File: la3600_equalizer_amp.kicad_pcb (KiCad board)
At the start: 2 copper layers, 90.9 x 174.8 mm, 70 parts, among them J1 JACK_TRS_3PINS, J2 JACK_TRS_3PINS, J3 Conn_01x03, Q1 BD139, Q2 BD140, Q3 BD139, Q4 BD140, U1 LA3600, U2 LA3600, U3 NE5532

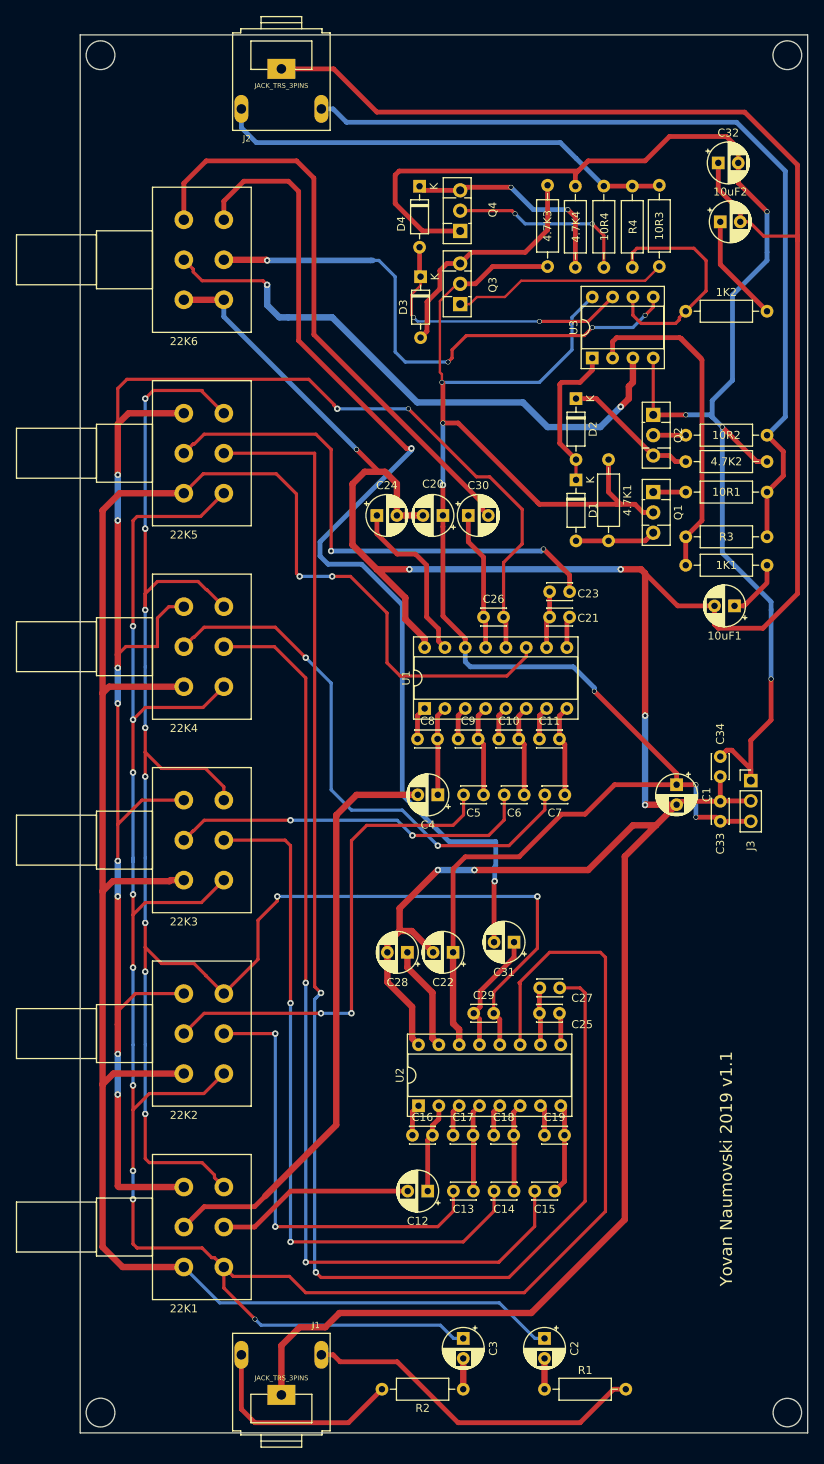
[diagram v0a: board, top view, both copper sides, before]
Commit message: add proper mounting holes (M3)
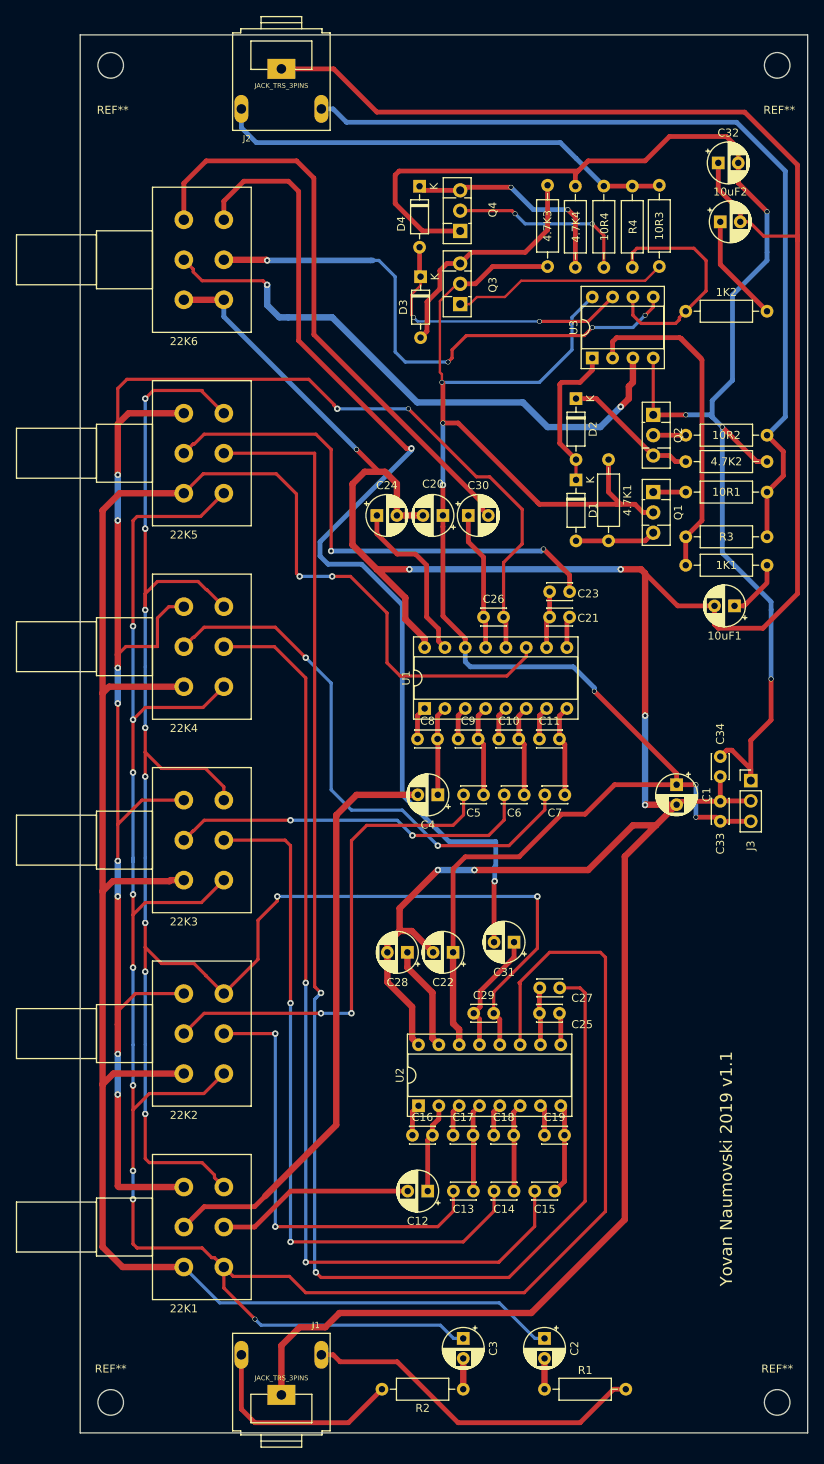
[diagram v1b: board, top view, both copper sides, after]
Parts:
- added REF**: MountingHole_3.2mm_M3, MountingHole:MountingHole_3.2mm_M3, F.Cu at (27.7, 28.4)
- added REF**: MountingHole_3.2mm_M3, MountingHole:MountingHole_3.2mm_M3, F.Cu at (111.0, 28.4)
- added REF**: MountingHole_3.2mm_M3, MountingHole:MountingHole_3.2mm_M3, F.Cu at (111.0, 195.6)
- added REF**: MountingHole_3.2mm_M3, MountingHole:MountingHole_3.2mm_M3, F.Cu at (27.7, 195.6)
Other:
- outline, holes or cut-outs redrawn
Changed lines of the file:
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@@
   (general
     (thickness 1.6)
-    (drawings 9)
+    (drawings 5)
     (tracks 761)
     (zones 0)
-    (modules 70)
+    (modules 74)
     (nets 66)
   )
@@
     )
   )
-  (gr_circle (center 112.268 196.85) (end 112.268 198.628) (layer Edge.Cuts) (width 0.15))
-  (gr_circle (center 26.416 196.85) (end 26.162 198.628) (layer Edge.Cuts) (width 0.15))
-  (gr_circle (center 112.268 27.178) (end 113.538 25.908) (layer Edge.Cuts) (width 0.15))
-  (gr_circle (center 26.416 27.178) (end 25.146 25.908) (layer Edge.Cuts) (width 0.15))
+  (module MountingHole:MountingHole_3.2mm_M3 (layer F.Cu)
+    (at 27.686 28.448)
+    (descr "Mounting Hole 3.2mm, no annular, M3")
+    (tags "mounting hole 3.2mm no annular m3")
+    (attr virtual)
+    (fp_text reference REF** (at 0.254 5.588) (layer F.SilkS)
+      (effects (font (size 1 1) (thickness 0.15)))
+    )
+    (fp_text value MountingHole_3.2mm_M3 (at 0 4.2) (layer F.Fab)
+      (effects (font (size 1 1) (thickness 0.15)))
+    )
+    (fp_circle (center 0 0) (end 3.45 0) (layer F.CrtYd) (width 0.05))
+    (fp_circle (center 0 0) (end 3.2 0) (layer Cmts.User) (width 0.15))
+    (fp_text user %R (at 0.3 0) (layer F.Fab)
+      (effects (font (size 1 1) (thickness 0.15)))
+    )
+    (pad 1 np_thru_hole circle (at 0 0) (size 3.2 3.2) (drill 3.2) (layers *.Cu *.Mask))
+  )
+  (module MountingHole:MountingHole_3.2mm_M3 (layer F.Cu)
+    (at 110.998 28.448)
+    (descr "Mounting Hole 3.2mm, no annular, M3")
+    (tags "mounting hole 3.2mm no annular m3")
+    (attr virtual)
+    (fp_text reference REF** (at 0.254 5.588) (layer F.SilkS)
+      (effects (font (size 1 1) (thickness 0.15)))
+    )
+    (fp_text value MountingHole_3.2mm_M3 (at 0 4.2) (layer F.Fab)
+      (effects (font (size 1 1) (thickness 0.15)))
+    )
+    (fp_circle (center 0 0) (end 3.45 0) (layer F.CrtYd) (width 0.05))
+    (fp_circle (center 0 0) (end 3.2 0) (layer Cmts.User) (width 0.15))
+    (fp_text user %R (at 0.3 0) (layer F.Fab)
+      (effects (font (size 1 1) (thickness 0.15)))
+    )
+    (pad 1 np_thru_hole circle (at 0 0) (size 3.2 3.2) (drill 3.2) (layers *.Cu *.Mask))
+  )
+  (module MountingHole:MountingHole_3.2mm_M3 (layer F.Cu)
+    (at 110.998 195.58)
+    (descr "Mounting Hole 3.2mm, no annular, M3")
+    (tags "mounting hole 3.2mm no annular m3")
+    (attr virtual)
+    (fp_text reference REF** (at 0 -4.2) (layer F.SilkS)
+      (effects (font (size 1 1) (thickness 0.15)))
+    )
+    (fp_text value MountingHole_3.2mm_M3 (at 0 4.2) (layer F.Fab)
+      (effects (font (size 1 1) (thickness 0.15)))
+    )
+    (fp_circle (center 0 0) (end 3.45 0) (layer F.CrtYd) (width 0.05))
+    (fp_circle (center 0 0) (end 3.2 0) (layer Cmts.User) (width 0.15))
+    (fp_text user %R (at 0.3 0) (layer F.Fab)
+      (effects (font (size 1 1) (thickness 0.15)))
+    )
+    (pad 1 np_thru_hole circle (at 0 0) (size 3.2 3.2) (drill 3.2) (layers *.Cu *.Mask))
+  )
+  (module MountingHole:MountingHole_3.2mm_M3 (layer F.Cu)
+    (at 27.686 195.58)
+    (descr "Mounting Hole 3.2mm, no annular, M3")
+    (tags "mounting hole 3.2mm no annular m3")
+    (attr virtual)
+    (fp_text reference REF** (at 0 -4.2) (layer F.SilkS)
+      (effects (font (size 1 1) (thickness 0.15)))
+    )
+    (fp_text value MountingHole_3.2mm_M3 (at 0 4.2) (layer F.Fab)
+      (effects (font (size 1 1) (thickness 0.15)))
+    )
+    (fp_circle (center 0 0) (end 3.45 0) (layer F.CrtYd) (width 0.05))
+    (fp_circle (center 0 0) (end 3.2 0) (layer Cmts.User) (width 0.15))
+    (fp_text user %R (at 0.3 0) (layer F.Fab)
+      (effects (font (size 1 1) (thickness 0.15)))
+    )
+    (pad 1 np_thru_hole circle (at 0 0) (size 3.2 3.2) (drill 3.2) (layers *.Cu *.Mask))
+  )
   (gr_text "Yovan Naumovski 2019 v1.1" (at 104.648 166.37 90) (layer F.SilkS)
     (effects (font (size 1.5 1.5) (thickness 0.3)))
